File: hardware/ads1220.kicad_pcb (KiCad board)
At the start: 2 copper layers, 39 parts, among them J1 Conn_01x04_Female, J2 Conn_01x04_Female, U1 LM4140-1.25, U2 MIC5205-2.5YM5, U3 ADS1220

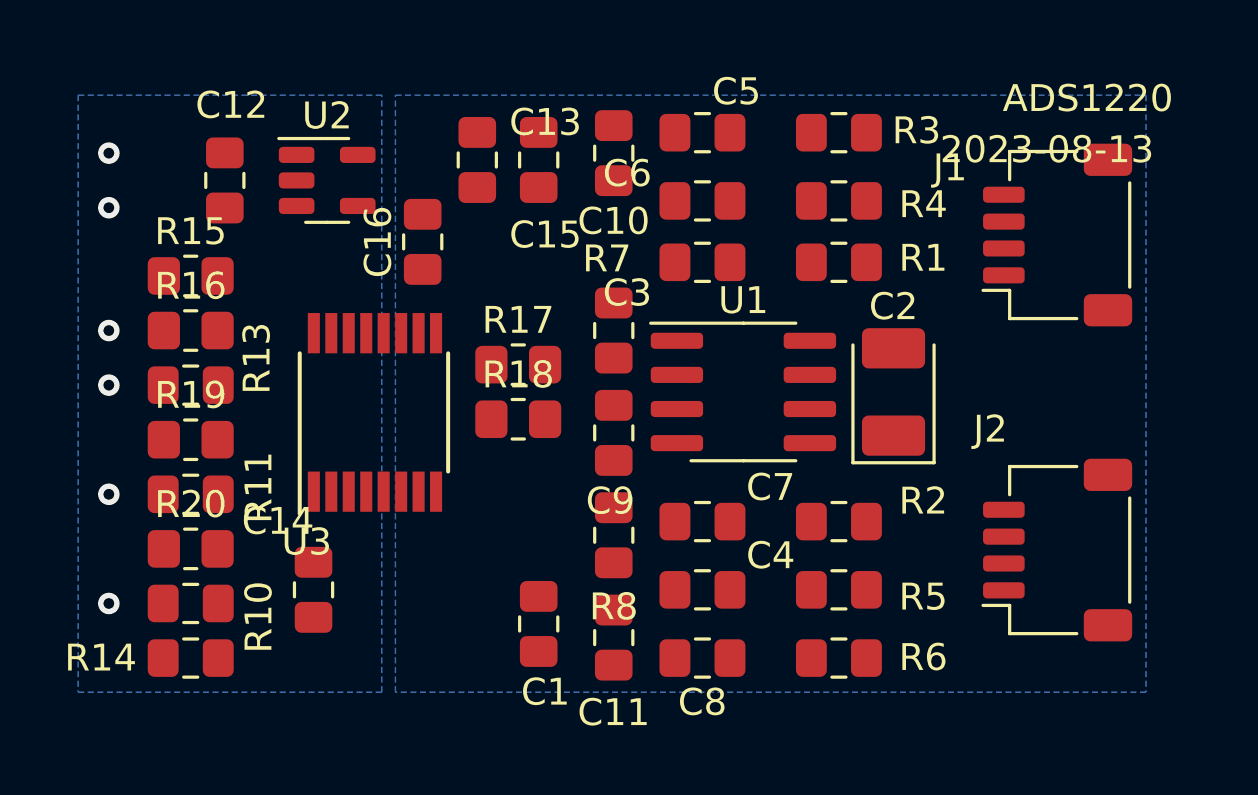
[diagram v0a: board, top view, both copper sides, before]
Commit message: datasheets and PCB mod to molex-minifit connector
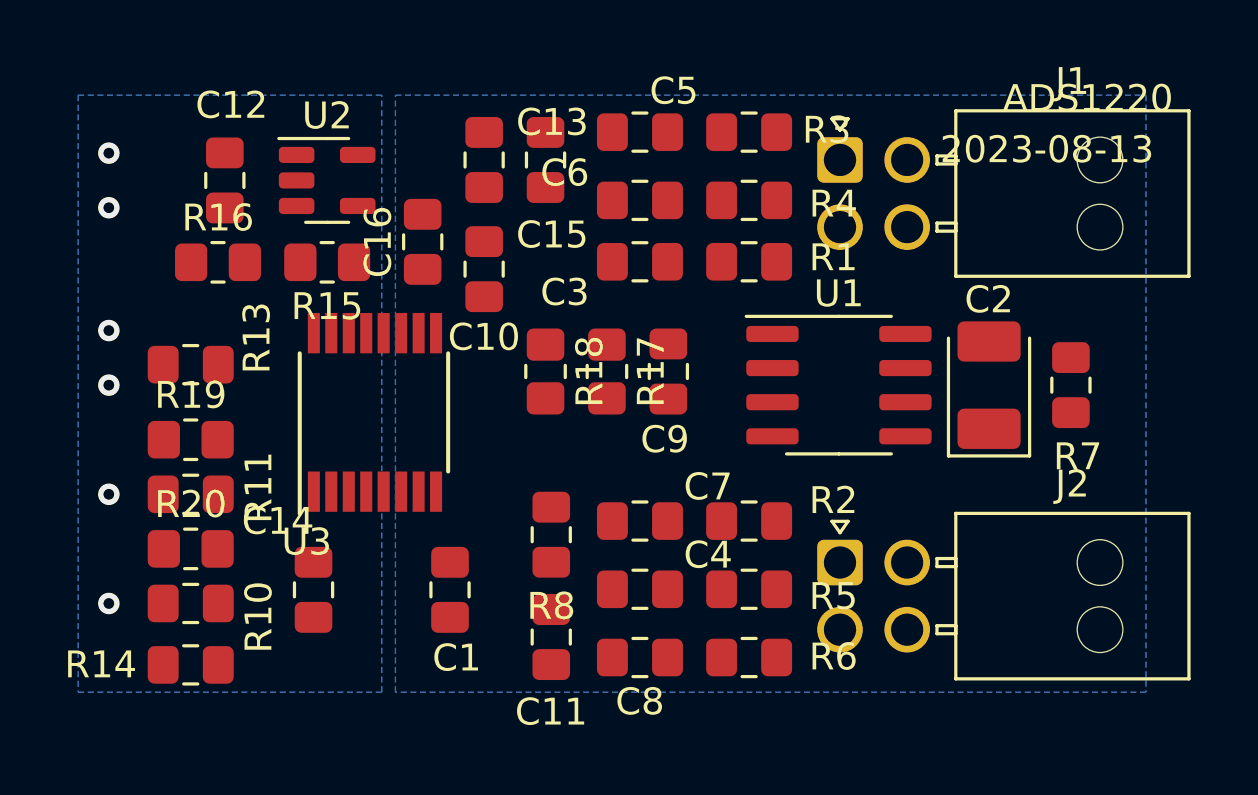
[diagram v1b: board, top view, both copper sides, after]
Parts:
- J1, J2: footprint Connector_JST:JST_SH_SM04B-SRSS-TB_1x04-1MP_P1.00mm_Horizontal -> Connector_Molex:Molex_Nano-Fit_105314-xx04_2x02_P2.50mm_Horizontal
- moved R7 17.1 mm to (158.5, 86.4), turned to 90 degrees
- moved J1 8.57 mm to (149.9, 78.0), turned to 0 degrees
- moved J2 8.11 mm to (149.9, 93.0), turned to 0 degrees
- moved C10 6.48 mm to (136.7, 82.0)
- moved R15 5.11 mm to (130.8, 81.8), turned to 180 degrees
- moved C2 3.57 mm to (155.4, 86.4)
- moved U1 3.57 mm to (149.9, 86.4)
- moved C1 3.54 mm to (135.4, 94.0)
- moved R1 3.34 mm to (146.5, 81.8)
- moved R2 3.34 mm to (146.5, 91.4)
- moved R3 3.34 mm to (146.5, 76.9)
- moved R4 3.34 mm to (146.5, 79.5)
- moved R5 3.34 mm to (146.5, 94.0)
- moved R6 3.34 mm to (146.5, 96.5)
- moved R17 3.31 mm to (141.2, 85.9), turned to -90 degrees
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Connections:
- J1 pad 1: Net-(J1-Pad1) -> Net-(J1-Pin_1)
- J1 pad 2: Net-(J1-Pad2) -> Net-(J1-Pin_2)
- J1 pad 3: Net-(J1-Pad3) -> Net-(J1-Pin_3)
- J1 pad 4: Net-(J1-Pad4) -> Net-(J1-Pin_4)
- J2 pad 1: Net-(J1-Pad1) -> Net-(J1-Pin_1)
- J2 pad 2: Net-(J1-Pad2) -> Net-(J1-Pin_2)
- J2 pad 3: Net-(J2-Pad3) -> Net-(J2-Pin_3)
- J2 pad 4: Net-(J2-Pad4) -> Net-(J2-Pin_4)
- U3 pad 10: Net-(C10-Pad2) -> Net-(U3-AIN1)
- U3 pad 11: Net-(C10-Pad1) -> Net-(U3-AIN0/REFP1)
- U3 pad 14: Net-(R13-Pad2) -> Net-(U3-~{DRDY})
- U3 pad 15: Net-(R11-Pad2) -> Net-(U3-DOUT/~{DRDY})
- U3 pad 16: Net-(R10-Pad2) -> Net-(U3-DIN)
- U3 pad 3: Net-(R14-Pad2) -> Net-(U3-CLK)
- U3 pad 6: Net-(C11-Pad2) -> Net-(U3-AIN3/REFN1)
- U3 pad 7: Net-(C11-Pad1) -> Net-(U3-AIN2)
- U3 pad 8: Net-(C4-Pad1) -> Net-(U3-REFN0)
- U3 pad 9: Net-(C3-Pad2) -> Net-(U3-REFP0)

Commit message: hardware updates
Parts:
- C1, C12, C13, C14: value C_Small -> 100n; footprint Capacitor_SMD:C_0805_2012Metric_Pad1.15x1.40mm_HandSolder -> Capacitor_SMD:C_0805_2012Metric_Pad1.18x1.45mm_HandSolder
- C10, C11, C3, C7, C9: value C_Small -> 10n; footprint Capacitor_SMD:C_0805_2012Metric_Pad1.15x1.40mm_HandSolder -> Capacitor_SMD:C_0805_2012Metric_Pad1.18x1.45mm_HandSolder
- C15: value C_Small -> 2u2; footprint Capacitor_SMD:C_0805_2012Metric_Pad1.15x1.40mm_HandSolder -> Capacitor_SMD:C_0805_2012Metric_Pad1.18x1.45mm_HandSolder
- C2: value CP_Small -> 10u; footprint Capacitor_Tantalum_SMD:CP_EIA-3528-15_AVX-H_Pad1.50x2.35mm_HandSolder -> Capacitor_SMD:C_0805_2012Metric_Pad1.18x1.45mm_HandSolder
- C4, C5, C6, C8: value C_Small -> 10n; footprint Resistor_SMD:R_0805_2012Metric_Pad1.15x1.40mm_HandSolder -> Capacitor_SMD:C_0805_2012Metric_Pad1.18x1.45mm_HandSolder
- R1: value R_Small -> 0; footprint Capacitor_SMD:C_0805_2012Metric_Pad1.15x1.40mm_HandSolder -> Resistor_SMD:R_0805_2012Metric_Pad1.20x1.40mm_HandSolder
- R10, R11, R13: value R_Small -> 100; footprint Resistor_SMD:R_0805_2012Metric_Pad1.15x1.40mm_HandSolder -> Resistor_SMD:R_0805_2012Metric_Pad1.20x1.40mm_HandSolder
- R14: value R_Small -> 10k; footprint Capacitor_SMD:C_0805_2012Metric_Pad1.15x1.40mm_HandSolder -> Resistor_SMD:R_0805_2012Metric_Pad1.20x1.40mm_HandSolder
- R2, R7, R8: value R_Small -> 0; footprint Resistor_SMD:R_0805_2012Metric_Pad1.15x1.40mm_HandSolder -> Resistor_SMD:R_0805_2012Metric_Pad1.20x1.40mm_HandSolder
- R3, R4, R6: value R_Small -> 10; footprint Capacitor_SMD:C_0805_2012Metric_Pad1.15x1.40mm_HandSolder -> Resistor_SMD:R_0805_2012Metric_Pad1.20x1.40mm_HandSolder
- R5: value R_Small -> 10; footprint Resistor_SMD:R_0805_2012Metric_Pad1.15x1.40mm_HandSolder -> Resistor_SMD:R_0805_2012Metric_Pad1.20x1.40mm_HandSolder
- moved C1 5.93 mm to (136.4, 88.1)
- moved R14 5.34 mm to (131.1, 97.0), turned to 0 degrees
- moved R10 4.06 mm to (125.7, 90.4)
- moved R19 4.06 mm to (125.7, 92.5), turned to 180 degrees
- moved R20 4.06 mm to (125.7, 88.4), turned to 180 degrees
- moved C9 4.06 mm to (139.4, 85.9)
- moved R11 4.06 mm to (125.7, 94.5)
- moved C16 3.05 mm to (134.4, 78.0)
- moved R18 3.05 mm to (142.0, 85.9)
- moved R17 2.79 mm to (144.0, 85.9)
- moved R15 0.51 mm to (130.3, 81.8)
- moved R16 0.51 mm to (126.2, 81.8)
- moved U3 0.51 mm to (132.6, 87.9)
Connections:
- C10 pad 1: Net-(C10-Pad1) -> Net-(U3-AIN0/REFP1)
- C10 pad 2: Net-(C10-Pad2) -> Net-(U3-AIN1)
- C11 pad 1: Net-(C11-Pad1) -> Net-(U3-AIN2)
- C11 pad 2: Net-(C11-Pad2) -> Net-(U3-AIN3/REFN1)
- C3 pad 2: Net-(C3-Pad2) -> Net-(U3-REFP0)
- C4 pad 1: Net-(C4-Pad1) -> Net-(U3-REFN0)
- C5 pad 2: Net-(C10-Pad1) -> Net-(U3-AIN0/REFP1)
- C6 pad 1: Net-(C10-Pad2) -> Net-(U3-AIN1)
- C7 pad 2: Net-(C11-Pad1) -> Net-(U3-AIN2)
- C8 pad 1: Net-(C11-Pad2) -> Net-(U3-AIN3/REFN1)
- C9 pad 1: Net-(C3-Pad2) -> Net-(U3-REFP0)
- C9 pad 2: Net-(C4-Pad1) -> Net-(U3-REFN0)
- J2 pad 1: Net-(J1-Pin_1) -> Net-(J2-Pin_1)
- J2 pad 2: Net-(J1-Pin_2) -> Net-(J2-Pin_2)
- J2 pad 3: Net-(J2-Pin_3) -> Net-(J1-Pin_3)
- J2 pad 4: Net-(J2-Pin_4) -> Net-(J1-Pin_4)
- R1 pad 1: Net-(C3-Pad2) -> Net-(U3-REFP0)
- R1 pad 2: Net-(J1-Pad2) -> Net-(J1-Pin_3)
- R10 pad 2: Net-(R10-Pad2) -> Net-(U3-DIN)
- R11 pad 2: Net-(R11-Pad2) -> Net-(U3-DOUT/~{DRDY})
- R13 pad 2: Net-(R13-Pad2) -> Net-(U3-~{DRDY})
- R14 pad 2: Net-(R14-Pad2) -> Net-(U3-CLK)
- R2 pad 1: Net-(C4-Pad1) -> Net-(U3-REFN0)
- R2 pad 2: Net-(J1-Pad1) -> Net-(J1-Pin_4)
- R3 pad 1: Net-(C10-Pad1) -> Net-(U3-AIN0/REFP1)
- R3 pad 2: Net-(J1-Pad4) -> Net-(J1-Pin_1)
- R4 pad 1: Net-(C10-Pad2) -> Net-(U3-AIN1)
- R4 pad 2: Net-(J1-Pad3) -> Net-(J1-Pin_2)
- R5 pad 1: Net-(C11-Pad1) -> Net-(U3-AIN2)
- R5 pad 2: Net-(J2-Pad4) -> Net-(J2-Pin_1)
- R6 pad 1: Net-(C11-Pad2) -> Net-(U3-AIN3/REFN1)
- R6 pad 2: Net-(J2-Pad3) -> Net-(J2-Pin_2)
- R7 pad 2: Net-(C3-Pad2) -> Net-(U3-REFP0)
- R8 pad 1: Net-(C4-Pad1) -> Net-(U3-REFN0)
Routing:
- net Vin: track 0.00 -> 43.5 mm
- net Net-(J1-Pin_4): track 0.00 -> 33.8 mm
- net +2V5: track 0.00 -> 33.4 mm
- net Net-(J1-Pin_3): track 0.00 -> 32.3 mm
- net GNDA: track 0.00 -> 29.9 mm, vias 0 -> 8
- net Net-(U3-REFP0): track 0.00 -> 27.9 mm
- net EN: track 0.00 -> 24.6 mm, vias 1 -> 3
- net 0V: track 0.00 -> 21.4 mm, vias 1 -> 3
- net Net-(U3-AIN0/REFP1): track 0.00 -> 16.7 mm
- net Net-(U3-AIN3/REFN1): track 0.00 -> 16.6 mm
- net Net-(U3-REFN0): track 0.00 -> 16.1 mm
- net Net-(U3-AIN1): track 0.00 -> 15.3 mm
- net Net-(U3-AIN2): track 0.00 -> 14.3 mm
- net Net-(U3-DOUT/~{DRDY}): track 0.00 -> 11.3 mm
- net Net-(U3-~{DRDY}): track 0.00 -> 7.28 mm
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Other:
- board text added: "2024-01-25"
- board text removed: "2023-08-13"

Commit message: commit PCB
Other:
- rule pad_to_mask_clearance: 0.051 -> 0
- board text added: "0V"
- board text added: "3v3"
- board text added: "C"
- board text added: "E"
- board text added: "I2C: 0x40"
- board text added: "R"
- board text added: "SDA"
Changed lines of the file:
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@@
   )
   (setup
-    (pad_to_mask_clearance 0.051)
+    (pad_to_mask_clearance 0)
     (solder_mask_min_width 0.25)
     (pcbplotparams
-      (layerselection 0x00021f0_ffffffff)
+      (layerselection 0x00021e0_ffffffff)
       (plot_on_all_layers_selection 0x0000000_00000000)
       (disableapertmacros false)
@@
       (dashed_line_gap_ratio 3.000000)
       (svgprecision 6)
-      (plotframeref true)
+      (plotframeref false)
       (viasonmask true)
       (mode 1)
@@
       (sketchpadsonfab false)
       (subtractmaskfromsilk false)
-      (outputformat 4)
+      (outputformat 1)
       (mirror false)
       (drillshape 0)
@@
     (property "Sheetname" "")
     (attr smd)
-    (fp_text reference "U3" (at -4.826 -2.54 180) (layer "F.SilkS")
+    (fp_text reference "U3" (at -4.064 -4.064 180) (layer "F.SilkS")
         (effects (font (size 1 1) (thickness 0.15)))
     )
@@
     (property "ki_keywords" "R resistor")
     (attr smd)
-    (fp_text reference "R3" (at 1.311 -1.65) (layer "F.SilkS")
+    (fp_text reference "R3" (at 1.311 -1.504) (layer "F.SilkS")
         (effects (font (size 1 1) (thickness 0.15)))
     )
@@
     (property "ki_keywords" "R resistor")
     (attr smd)
-    (fp_text reference "R11" (at -1.524 1.778) (layer "F.SilkS")
+    (fp_text reference "R11" (at 1.524 1.778) (layer "F.SilkS")
         (effects (font (size 1 1) (thickness 0.15)))
     )
@@
     (property "ki_keywords" "R resistor")
     (attr smd)
-    (fp_text reference "R10" (at -3.286 -1.016) (layer "F.SilkS")
+    (fp_text reference "R10" (at 2.556 -0.762 90) (layer "F.SilkS")
         (effects (font (size 1 1) (thickness 0.15)))
     )
@@
     (property "Sheetname" "")
     (attr smd)
-    (fp_text reference "C2" (at 0 -1.68 90) (layer "F.SilkS")
+    (fp_text reference "C2" (at 2.794 1.27 90) (layer "F.SilkS")
         (effects (font (size 1 1) (thickness 0.15)))
     )
@@
     (property "ki_keywords" "150mA low-noise LDO linear voltage regulator fixed positive")
     (attr smd)
-    (fp_text reference "U2" (at 0 -2.4) (layer "F.SilkS")
+    (fp_text reference "U2" (at 1.016 -2.286) (layer "F.SilkS")
         (effects (font (size 1 1) (thickness 0.15)))
     )
@@
     (property "ki_keywords" "capacitor cap")
     (attr smd)
-    (fp_text reference "C12" (at 0 1.778 -90) (layer "F.SilkS")
+    (fp_text reference "C12" (at 0.254 1.524 90) (layer "F.SilkS")
         (effects (font (size 1 1) (thickness 0.15)))
     )
@@
     (property "ki_keywords" "capacitor cap")
     (attr smd)
-    (fp_text reference "C14" (at -2.032 -2.54 180) (layer "F.SilkS")
+    (fp_text reference "C14" (at -1.016 2.54 180) (layer "F.SilkS")
         (effects (font (size 1 1) (thickness 0.15)))
     )
@@
     (property "ki_keywords" "R resistor")
     (attr smd)
-    (fp_text reference "R7" (at 0 -1.65 90) (layer "F.SilkS")
+    (fp_text reference "R7" (at 0.254 1.778 90) (layer "F.SilkS")
         (effects (font (size 1 1) (thickness 0.15)))
     )
@@
     (property "ki_keywords" "R resistor")
     (attr smd)
-    (fp_text reference "R14" (at 2.54 -1.524) (layer "F.SilkS")
+    (fp_text reference "R14" (at 3.302 0) (layer "F.SilkS")
         (effects (font (size 1 1) (thickness 0.15)))
     )
@@
     (property "ki_keywords" "R resistor")
     (attr smd)
-    (fp_text reference "R17" (at 2.286 0) (layer "F.SilkS")
+    (fp_text reference "R17" (at 2.54 0.254) (layer "F.SilkS")
         (effects (font (size 1 1) (thickness 0.15)))
     )
@@
     (property "ki_keywords" "R resistor")
     (attr smd)
-    (fp_text reference "R20" (at 3.302 0.254) (layer "F.SilkS")
+    (fp_text reference "R20" (at 3.048 0.254) (layer "F.SilkS")
         (effects (font (size 1 1) (thickness 0.15)))
     )
@@
     (property "ki_keywords" "R resistor")
     (attr smd)
-    (fp_text reference "R18" (at 2.286 1.016 -180) (layer "F.SilkS")
+    (fp_text reference "R18" (at 2.54 1.524 -180) (layer "F.SilkS")
         (effects (font (size 1 1) (thickness 0.15)))
     )
@@
   (gr_line (start 121 74.746) (end 164 74.746)
     (stroke (width 0.15) (type solid)) (layer "Dwgs.User"))
-  (gr_text "ADS1220" (at 125.476 75.946) (layer "F.SilkS")
+  (gr_text "0V" (at 123.952 80.518) (layer "F.SilkS")
     (effects (font (size 1 1) (thickness 0.15)))
   )
+  (gr_text "3v3" (at 122.682 76.2) (layer "F.SilkS")
+    (effects (font (size 1 1) (thickness 0.15)))
+  )
+  (gr_text "R" (at 121.666 85.344) (layer "F.SilkS")
+    (effects (font (size 1 1) (thickness 0.15)))
+  )
+  (gr_text "SDA" (at 122.936 96.266) (layer "F.SilkS")
+    (effects (font (size 1 1) (thickness 0.15)))
+  )
+  (gr_text "ADS1220" (at 127.762 75.692) (layer "F.SilkS")
+    (effects (font (size 1 1) (thickness 0.15)))
+  )
+  (gr_text "C" (at 121.666 89.408) (layer "F.SilkS")
+    (effects (font (size 1 1) (thickness 0.15)))
+  )
+  (gr_text "I2C: 0x40" (at 125.222 98.044) (layer "F.SilkS")
+    (effects (font (size 1 1) (thickness 0.15)))
+  )
   (gr_text "2024-01-25" (at 154.686 89.916) (layer "F.SilkS")
+    (effects (font (size 1 1) (thickness 0.15)))
+  )
+  (gr_text "E" (at 121.92 83.058) (layer "F.SilkS")
     (effects (font (size 1 1) (thickness 0.15)))
   )
@@
   (segment (start 129.6725 77.79) (end 130.056751 77.79) (width 0.25) (layer "F.Cu") (net 4))
   (segment (start 126.9785 77.724) (end 127 77.7025) (width 0.25) (layer "F.Cu") (net 4))
-  (via (at 122.682 77.724) (size 0.8) (drill 0.4) (layers "F.Cu" "B.Cu") (net 4))
+  (via (at 122.682 77.724) (size 1.5) (drill 0.8) (layers "F.Cu" "B.Cu") (net 4))
   (segment (start 130.302 92.9425) (end 130.302 92.9425) (width 0.25) (layer "F.Cu") (net 5))
   (segment (start 130.302 90.845) (end 130.313 90.834) (width 0.25) (layer "F.Cu") (net 5))
@@
   (segment (start 126.9785 79.756) (end 127 79.7775) (width 0.25) (layer "F.Cu") (net 5))
   (via (at 132.337077 93.472) (size 0.8) (drill 0.4) (layers "F.Cu" "B.Cu") (net 5))
-  (via (at 122.682 79.756) (size 0.8) (drill 0.4) (layers "F.Cu" "B.Cu") (net 5))
+  (via (at 122.682 79.756) (size 1.5) (drill 0.8) (layers "F.Cu" "B.Cu") (net 5))
   (via (at 128.524 93.98) (size 0.8) (drill 0.4) (layers "F.Cu" "B.Cu") (free) (net 5))
   (segment (start 148.904 93.96) (end 149.9 92.964) (width 0.25) (layer "F.Cu") (net 6))
@@
   (segment (start 122.682 86.36) (end 123.968 86.36) (width 0.25) (layer "F.Cu") (net 8))
   (segment (start 123.968 86.36) (end 124.73 85.598) (width 0.25) (layer "F.Cu") (net 8))
-  (via (at 122.682 86.36) (size 0.8) (drill 0.4) (layers "F.Cu" "B.Cu") (net 8))
+  (via (at 122.682 86.36) (size 1.5) (drill 0.8) (layers "F.Cu" "B.Cu") (net 8))
   (segment (start 133.679 79.69) (end 134.366 79.003) (width 0.25) (layer "F.Cu") (net 9))
   (segment (start 131.9475 79.69) (end 133.679 79.69) (width 0.25) (layer "F.Cu") (net 9))
@@
   (via (at 125.222 83.312) (size 0.8) (drill 0.4) (layers "F.Cu" "B.Cu") (net 10))
   (via (at 143.324497 83.380497) (size 0.8) (drill 0.4) (layers "F.Cu" "B.Cu") (net 10))
-  (via (at 122.682 84.328) (size 0.8) (drill 0.4) (layers "F.Cu" "B.Cu") (net 10))
+  (via (at 122.682 84.328) (size 1.5) (drill 0.8) (layers "F.Cu" "B.Cu") (net 10))
   (segment (start 143.324497 83.380497) (end 143.256 83.312) (width 0.25) (layer "B.Cu") (net 10))
   (segment (start 143.256 83.312) (end 125.222 83.312) (width 0.25) (layer "B.Cu") (net 10))
@@
   (segment (start 124.73 92.456) (end 124.73 94.488) (width 0.25) (layer "F.Cu") (net 15))
   (segment (start 122.682 94.488) (end 124.73 94.488) (width 0.25) (layer "F.Cu") (net 15))
-  (via (at 122.682 94.488) (size 0.8) (drill 0.4) (layers "F.Cu" "B.Cu") (free) (net 15))
+  (via (at 122.682 94.488) (size 1.5) (drill 0.8) (layers "F.Cu" "B.Cu") (free) (net 15))
   (segment (start 124.714 90.424) (end 124.714 88.392) (width 0.25) (layer "F.Cu") (net 16))
   (segment (start 124.714 90.399) (end 124.689 90.424) (width 0.25) (layer "F.Cu") (net 16))
   (segment (start 122.666 90.424) (end 124.714 90.424) (width 0.25) (layer "F.Cu") (net 16))
-  (via (at 122.666 90.424) (size 0.8) (drill 0.4) (layers "F.Cu" "B.Cu") (free) (net 16))
+  (via (at 122.666 90.424) (size 1.5) (drill 0.8) (layers "F.Cu" "B.Cu") (free) (net 16))
   (segment (start 129.302 80.756) (end 129.302 81.788) (width 0.25) (layer "F.Cu") (net 17))
   (segment (start 129.6725 80.3855) (end 129.302 80.756) (width 0.25) (layer "F.Cu") (net 17))
